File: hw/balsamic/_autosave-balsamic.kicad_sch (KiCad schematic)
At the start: 50 parts, among them J1 Conn_01x24, J3 USB_B_Mini, SW1 SW_Push, U1 ISP1807-LR-RS, U2 BMI160, U4 MAX77658AANX+

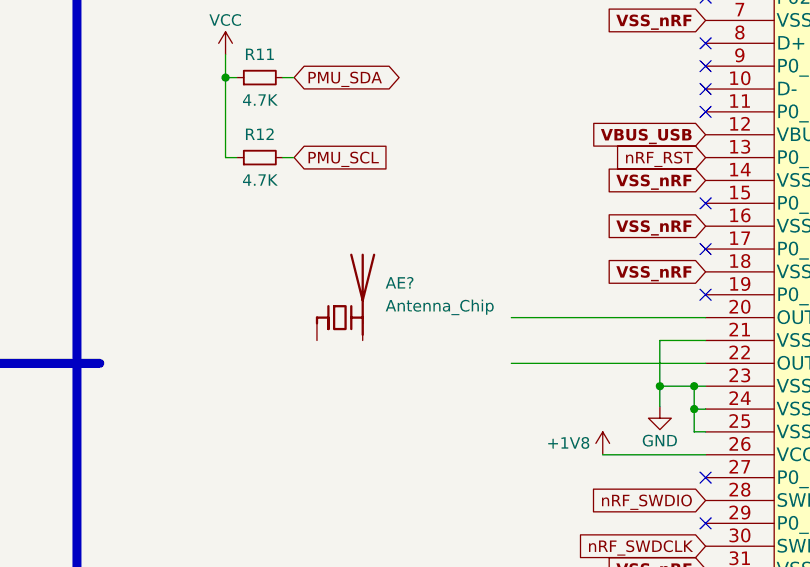
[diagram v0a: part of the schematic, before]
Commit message: began shrinking board w/out K210
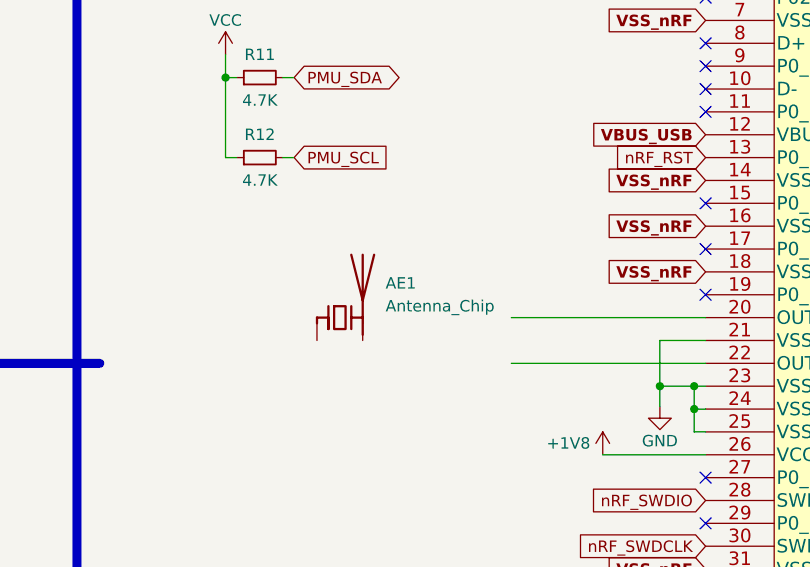
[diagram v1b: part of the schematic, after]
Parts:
- gave numbers to parts that had none: 1
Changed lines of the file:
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@@
   (symbol (lib_id "Device:Antenna_Chip") (at 138.43 195.58 0) (unit 1)
     (in_bom yes) (on_board yes) (fields_autoplaced)
-    (property "Reference" "AE?" (id 0) (at 143.51 191.7699 0)
+    (property "Reference" "AE1" (id 0) (at 143.51 191.7699 0)
       (effects (font (size 1.27 1.27)) (justify left))
     )
@@
     )
     (path "/5147e84e-9f67-44f1-8b73-f7047f2aa137"
-      (reference "AE?") (unit 1) (value "Antenna_Chip") (footprint "")
+      (reference "AE1") (unit 1) (value "Antenna_Chip") (footprint "")
     )
     (path "/34606f62-6626-40ba-a39d-83e52aa6dcc2"
